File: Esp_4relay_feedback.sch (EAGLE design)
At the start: 93 parts, among them IC1 LM1117MP-3.3, IC2 NE555, IC4 7805TV, K1 G5LE, K2 G5LE, K3 G5LE, K4 G5LE, K5 G5LE, K6 G5LE, K7 G5LE, K8 G5LE, Q1 16MHz, Q11 BC450, Q2 BC547, Q3 BC547, Q4 BC547, Q5 BC547, Q6 BC547, Q7 BC547, Q8 BC547, Q9 BC547, T1 2N7000, T2 2N7000, U2 ATMEGA328P_PDIP

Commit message: schematic change
feedback circuit connection changed
added tip127 to control relay power supply.
made separate supply for relay and controller.
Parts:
- removed Q3: BC547, transistor-npn:BC447
- added C10, C11: 10uf, rcl:CPOL-USE2.5-6
- added D9: 1N4004, amit_diode_1N4004:1N4004
- added IC3: 7805TV, linear:7805TV
- added JP2, JP3, JP4: (no value), pinhead:PINHD-1X2
- added JP5: (no value), pinhead:PINHD-1X4
- added JP9: (no value), pinhead:PINHD-1X5
- added Q10: BC547, transistor-npn:BC447
- added X11: (no value), amit_screw_terminal_23:W237-102
- added X6: (no value), con-wago-500:W237-103
- Q11: value BC450 -> TIP120; device transistor-pnp:BC450 -> transistor-power:TIP120
- R14, R8: value 1k -> 220k
- R15, R9: value 220k -> 1k
- X10: device con-wago-500:W237-103 -> amit_screw_terminal_23:W237-102; MPN 237-103 -> (none); OC_FARNELL unknown -> (none); OC_NEWARK 18M7116 -> (none)
- X7: device con-wago-500:W237-102 -> con-wago-500:W237-103; MPN (none) -> 237-103; OC_FARNELL (none) -> unknown; OC_NEWARK (none) -> 18M7116
- X9: device con-wago-500:W237-103 -> con-wago-500:W237-102; MPN 237-103 -> (none); OC_FARNELL unknown -> (none); OC_NEWARK 18M7116 -> (none)
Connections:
- removed net N$12 (its old number): D2.A, K21.2, Q3.C
- removed net N$18 (its old number): D3.A, K31.2, Q4.C
- removed net N$33 (its old number): C5.+, IC4.VI, X7-1.KL
- removed net N$35 (its old number): Q6.B, R7.1
- removed net N$61: D8.A, K81.2, Q9.C
- removed net VCC: C1.+, C2.+, IC1.IN, IC2./RES, IC2.VCC+, IC4.VO, Q11.E, R21.2, R22.2, R25.1, R27.1, R3.2, U2.AREF, U2.AVCC, U2.VCC
- new net 12V: C10.+, C5.+, D9.C, IC3.VI, IC4.VI
- new net LINE: OK1.C, OK2.C, OK3.C, OK4.C, OK5.C, OK6.C, OK7.C, OK8.C, X10-1.KL, X10-2.KL, X11-1.KL, X11-2.KL
- new net N$112: C11.+, IC3.VO, Q11.C
- new net N$30: OK4.A, R10.2
- new net N$31: K52.P, R14.1, X5-2.KL
- new net N$42: OK5.A, R14.2
- new net N$43: K62.P, R16.1, X6-2.KL
- new net N$44: K62.S, X6-1.KL
- new net N$45: Q8.B, R15.1
- new net N$50: K72.S, X7-1.KL
- new net N$62: JP3.1, U$1.GPIO14
- new net N$66: D9.A, X9-1.KL
- new net VCC1: C1.+, C2.+, IC1.IN, IC2./RES, IC2.VCC+, IC4.VO, JP9.4, R21.2, R22.2, R25.1, R27.1, R3.2, U2.AREF, U2.AVCC, U2.VCC
- net ERT: now also JP2.1
- net F2: now also U2.PD4(XCK/T0); no longer U2.PD5(T1)
- net F4: now also U2.PD2(INT0); no longer U2.PD3(INT1)
- net F7: now also U2.PB4(MISO); no longer U2.PB5(SCK)
- net GND: now also C10.-, C11.-, IC3.GND, JP5.1, JP5.2, JP5.3, JP5.4, JP9.5, Q10.E, X9-2.KL; no longer Q3.E, X7-2.KL
- net N$1: now also R2.1; no longer OK1.A
- net N$11: now also D2.A, K21.2, Q4.C; no longer Q3.B, R5.1
- net N$13: now also OK2.A, R6.2; no longer K32.P, OK3.A, X3-2.KL
- net N$14: now also K32.P, R8.1, X3-2.KL; no longer K32.S, R9.1, X3-1.KL
- net N$15: now also K32.S, X3-1.KL; no longer OK3.C, R9.2
- net N$16: now also Q5.B, R7.1; no longer K52.P, OK5.A, X5-2.KL
- net N$17: now also D3.A, K31.2, Q5.C; no longer Q4.B, R8.1
- net N$19: now also OK3.A, R8.2; no longer K42.P, OK4.A, X4-2.KL
- net N$2: now also OK1.A; no longer OK1.C
- net N$20: now also K42.P, R10.1, X4-2.KL; no longer K42.S, R15.1, X4-1.KL
- net N$22: now also K42.S, X4-1.KL; no longer OK4.C, R15.2
- net N$24: now also Q6.B, R9.1; no longer Q5.B, R14.1
- net N$25: now also Q6.C; no longer Q5.C
- net N$3: no longer R2.1
- net N$32: no longer R10.1
- net N$34: now also D5.A, K51.2, Q7.C; no longer OK5.C, R10.2
- net N$4: now also R6.1; no longer OK2.A
- net N$46: now also D6.A, K61.2, Q8.C; no longer D5.A, K51.2, Q6.C
- net N$47: now also K62.O, X6-3.KL; no longer K62.P, OK6.A, X8-2.KL
- net N$48: now also OK6.A, R16.2; no longer K62.S, R16.1, X8-1.KL
- net N$49: now also K72.P, R18.1, X7-2.KL; no longer OK6.C, R16.2
- net N$51: now also Q9.B, R17.1; no longer D6.A, K61.2, Q7.C
- net N$52: now also D7.A, K71.2, Q9.C; no longer K72.P, OK7.A, X9-2.KL
- net N$53: now also K72.O, X7-3.KL; no longer K72.S, R18.1, X9-1.KL
- net N$54: now also OK7.A; no longer OK7.C
- net N$55: now also K82.P, R20.1, X8-2.KL; no longer Q8.B, R17.1
- net N$56: now also K82.S, X8-1.KL; no longer D7.A, K71.2, Q8.C
- net N$57: now also Q10.B, R19.1; no longer K82.P, OK8.A, X10-2.KL
- net N$58: now also D8.A, K81.2, Q10.C; no longer K82.S, R20.1, X10-1.KL
- net N$59: now also K82.O, X8-3.KL; no longer OK8.C, R20.2
- net N$6: no longer R6.1
- net N$60: now also OK8.A, R20.2; no longer Q9.B, R19.1
- net N$63: now also JP3.2, U$1.GPIO16; no longer K62.O, X8-3.KL
- net N$64: now also JP4.1, U$1.GPIO13; no longer K72.O, X9-3.KL
- net N$65: now also JP4.2, U$1.GPIO12; no longer K82.O, X10-3.KL
- net N$9: now also Q4.B, R5.1; no longer OK2.C, R6.2
- net R2: now also U2.PD5(T1); no longer U2.PD4(XCK/T0)
- net R3: now also R7.2; no longer R8.2
- net R4: now also R9.2, U2.PD3(INT1); no longer R14.2, U2.PD2(INT0)
- net R5: now also R13.2; no longer R7.2
- net R6: now also R15.2; no longer R13.2
- net R7: now also U2.PB5(SCK); no longer U2.PB4(MISO)
- net RELAY_SUPPLY: now also Q11.E; no longer Q11.C
- net RESET: now also JP9.3
- net RX: now also JP9.1
- net TX: now also JP9.2
- net WE: now also JP2.2
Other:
- moved on the sheet: D1, D2, D3, D4, D5, D6, D7, D8, K1, K2, K3, K4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

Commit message: PDF
final pdf added.
developed PCB with this design
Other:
- moved on the sheet: X1-1
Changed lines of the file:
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@@
 <instance part="R2" gate="G$1" x="66.04" y="231.14" rot="R270"/>
 <instance part="GND2" gate="1" x="48.26" y="203.2"/>
-<instance part="X1" gate="-1" x="83.82" y="223.52" rot="R180"/>
+<instance part="X1" gate="-1" x="60.96" y="223.52" rot="R180"/>
 <instance part="X1" gate="-2" x="86.36" y="241.3" rot="R180"/>
 <instance part="X1" gate="-3" x="53.34" y="254" rot="R270"/>
@@
 <pinref part="K1" gate="2" pin="S"/>
 <wire x1="53.34" y1="236.22" x2="53.34" y2="223.52" width="0.1524" layer="91"/>
-<wire x1="53.34" y1="223.52" x2="78.74" y2="223.52" width="0.1524" layer="91"/>
+<wire x1="53.34" y1="223.52" x2="55.88" y2="223.52" width="0.1524" layer="91"/>
 <pinref part="X1" gate="-1" pin="KL"/>
 </segment>

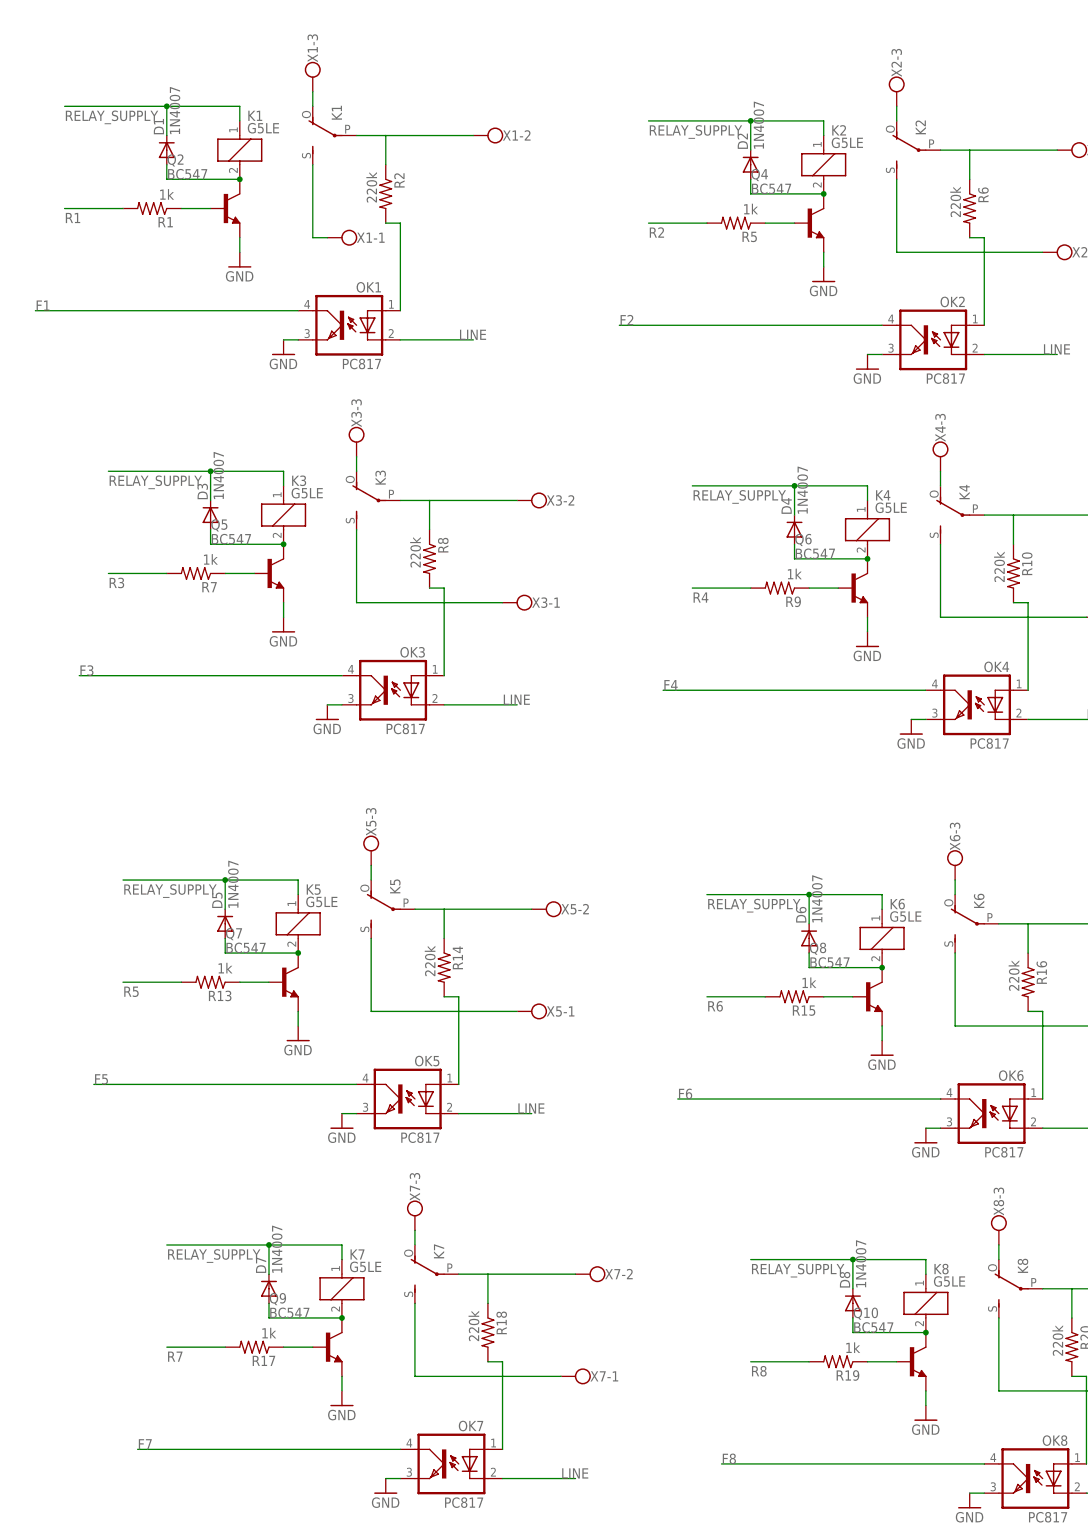
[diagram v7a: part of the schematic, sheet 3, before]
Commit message: schematic changes
EL814 pull up added.
HIGH LINK 5W supply added
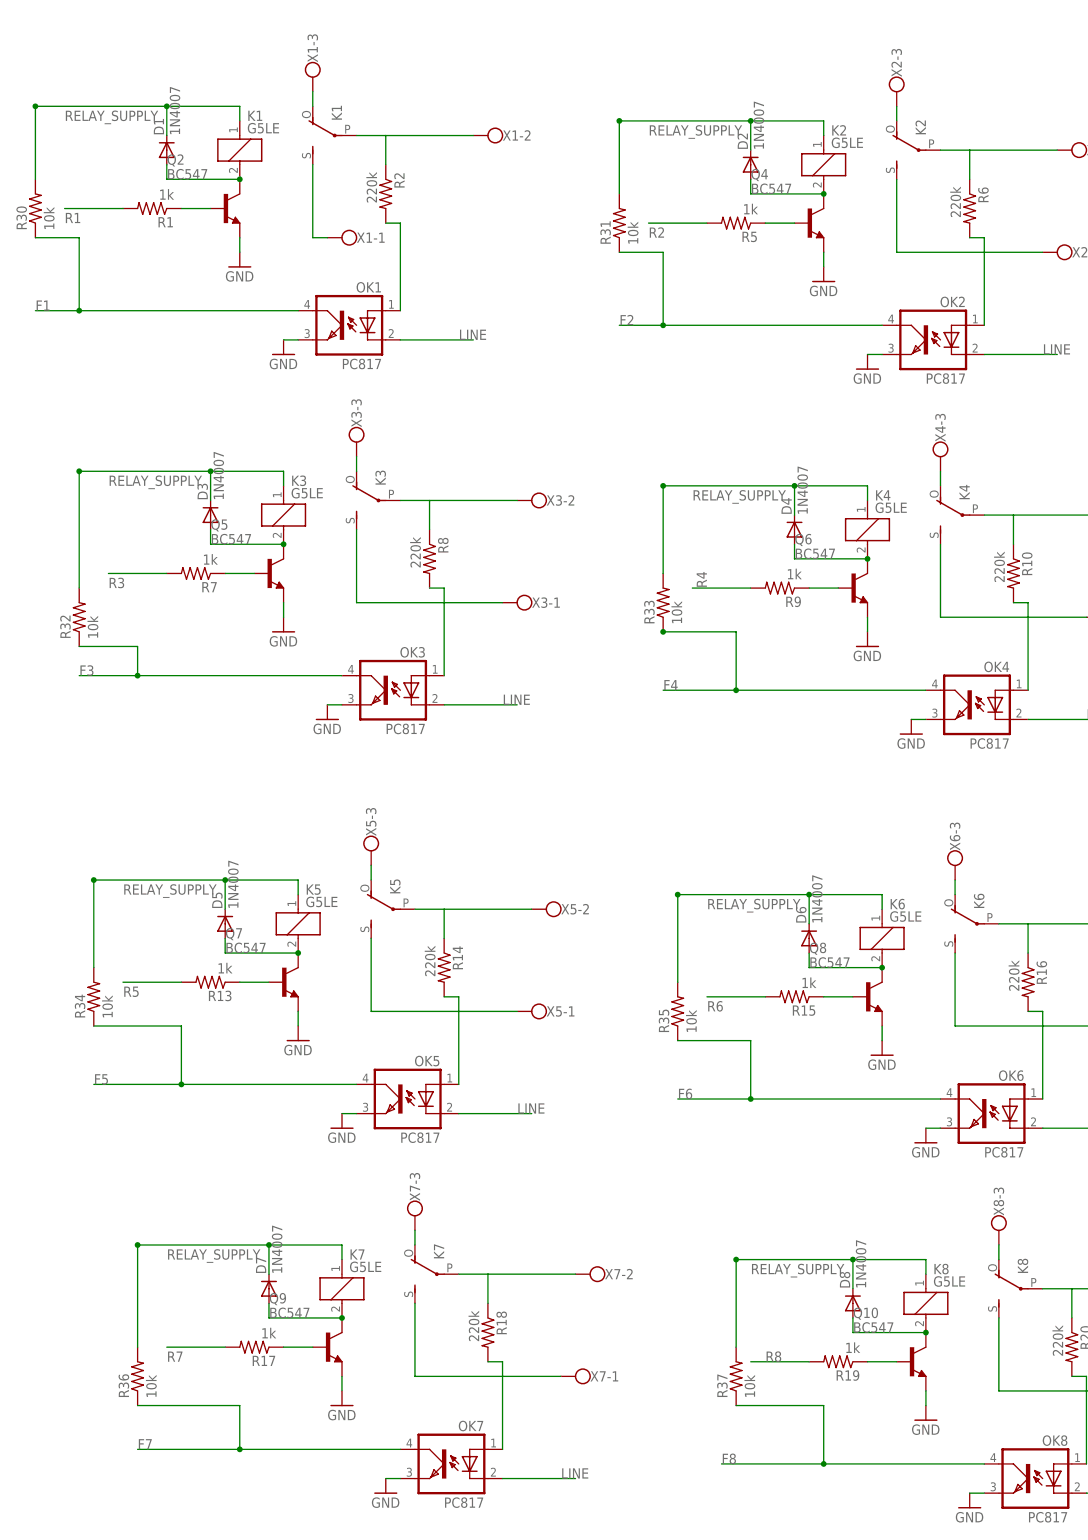
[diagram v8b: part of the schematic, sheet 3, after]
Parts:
- removed C1, C10, C11, C5: 10uf, rcl:CPOL-USE2.5-6
- removed D9: 1N4004, amit_diode_1N4004:1N4004
- removed IC3, IC4: 7805TV, linear:7805TV
- added R30, R31, R32, R33, R34, R35, R36, R37: 10k, amit_rcl:R-US_0207/5V
- added U$2: AMIT_HIGH_LINK, amit_high_link_5W:AMIT_HIGH_LINK
- X9: device con-wago-500:W237-102 -> amit_screw_terminal_23:W237-102
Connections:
- removed net 12V: C10.+, C5.+, D9.C, IC3.VI, IC4.VI
- removed net N$112: C11.+, IC3.VO, Q11.C
- new net N$61: U$2.AC1, X9-1.KL
- net F1: now also R30.1
- net F2: now also R31.1
- net F3: now also R32.1
- net F4: now also R33.1
- net F5: now also R34.1
- net F6: now also R35.1
- net F7: now also R36.1
- net F8: now also R37.1
- net GND: now also U$2.GND; no longer C1.-, C10.-, C11.-, C5.-, IC3.GND, IC4.GND, X9-2.KL
- net N$66: now also U$2.AC2, X9-2.KL; no longer D9.A, X9-1.KL
- net RELAY_SUPPLY: now also Q11.C, R30.2, R31.2, R32.2, R33.2, R34.2, R35.2, R36.2, R37.2; no longer Q11.E
- net VCC1: now also Q11.E, U$2.VCC; no longer C1.+, IC4.VO
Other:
- moved on the sheet: X9-1, X9-2
